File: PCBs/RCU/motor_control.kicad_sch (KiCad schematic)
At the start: 36 parts, among them U300 OPA365xxD, U301 DRV8876, U302 OPA365xxD, U303 DRV8876

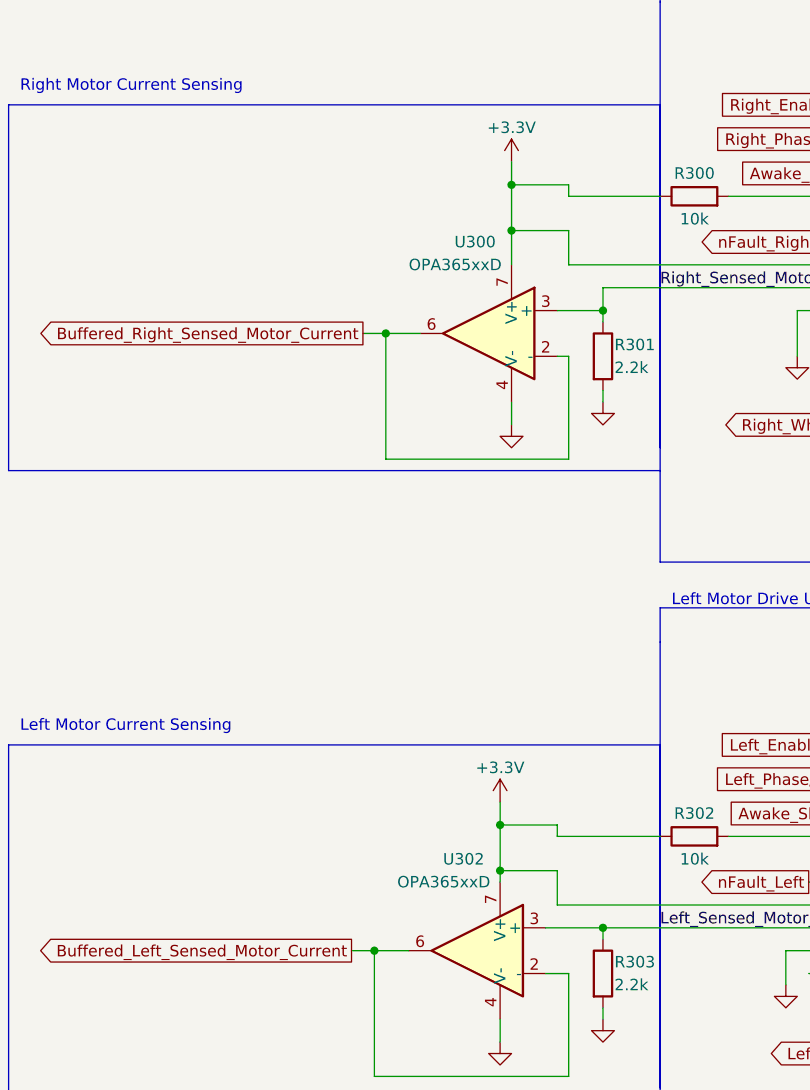
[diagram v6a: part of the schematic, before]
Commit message: Add 0.1uF bypass caps to Buffer in motor_control schematic
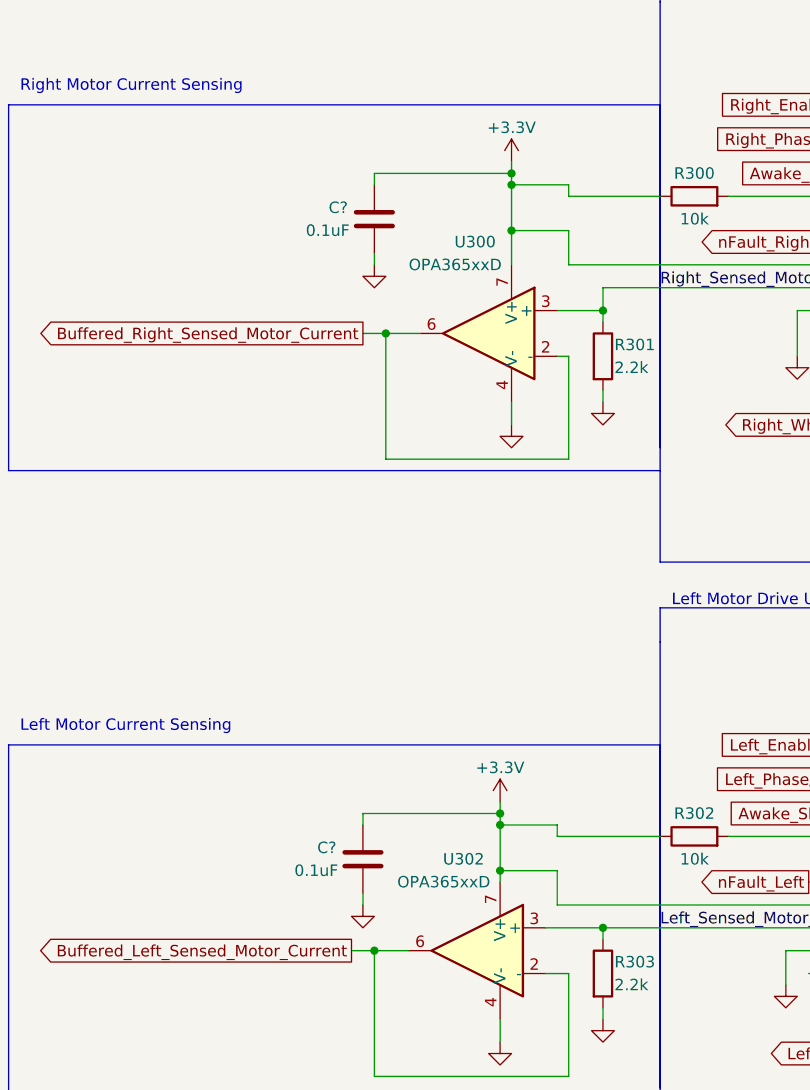
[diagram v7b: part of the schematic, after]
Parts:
- added C? (x2): 0.1uF, symbol Device:C
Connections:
- net +3V3: now also C?.1, C?.1
- net GND: now also C?.2, C?.2
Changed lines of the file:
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@@
   (junction (at 241.3 76.2) (diameter 0) (color 0 0 0 0)
   )
+  (junction (at 85.09 119.38) (diameter 0) (color 0 0 0 0)
+  )
   (junction (at 189.23 76.2) (diameter 0) (color 0 0 0 0)
   )
@@
   (junction (at 184.15 49.53) (diameter 0) (color 0 0 0 0)
   )
+  (junction (at 86.36 48.26) (diameter 0) (color 0 0 0 0)
+  )
   (junction (at 219.71 33.02) (diameter 0) (color 0 0 0 0)
   )
@@
     (stroke (width 0) (type default) (color 0 0 0 0))
   )
+  (wire (pts (xy 85.09 119.38) (xy 85.09 120.65))
+    (stroke (width 0) (type default) (color 0 0 0 0))
+  )
   (wire (pts (xy 193.04 146.05) (xy 193.04 147.32))
     (stroke (width 0) (type default) (color 0 0 0 0))
@@
     (stroke (width 0) (type default) (color 0 0 0 0))
   )
+  (wire (pts (xy 69.85 129.54) (xy 69.85 128.27))
+    (stroke (width 0) (type default) (color 0 0 0 0))
+  )
   (polyline (pts (xy 102.87 162.56) (xy 255.27 162.56))
     (stroke (width 0) (type default) (color 0 0 0 0))
@@
     (stroke (width 0) (type default) (color 0 0 0 0))
   )
+  (wire (pts (xy 71.12 48.26) (xy 86.36 48.26))
+    (stroke (width 0) (type default) (color 0 0 0 0))
+  )
   (wire (pts (xy 110.49 50.8) (xy 123.19 50.8))
     (stroke (width 0) (type default) (color 0 0 0 0))
@@
     (stroke (width 0) (type default) (color 0 0 0 0))
   )
+  (wire (pts (xy 69.85 119.38) (xy 85.09 119.38))
+    (stroke (width 0) (type default) (color 0 0 0 0))
+  )
   (wire (pts (xy 123.19 50.8) (xy 123.19 55.88))
     (stroke (width 0) (type default) (color 0 0 0 0))
@@
     (stroke (width 0) (type default) (color 0 0 0 0))
   )
+  (wire (pts (xy 86.36 48.26) (xy 86.36 49.53))
+    (stroke (width 0) (type default) (color 0 0 0 0))
+  )
   (polyline (pts (xy 30.48 40.64) (xy 102.87 40.64))
     (stroke (width 0) (type default) (color 0 0 0 0))
@@
     (stroke (width 0) (type default) (color 0 0 0 0))
   )
+  (wire (pts (xy 71.12 49.53) (xy 71.12 48.26))
+    (stroke (width 0) (type default) (color 0 0 0 0))
+  )
   (wire (pts (xy 189.23 132.08) (xy 189.23 134.62))
     (stroke (width 0) (type default) (color 0 0 0 0))
@@
     (stroke (width 0) (type default) (color 0 0 0 0))
   )
+  (wire (pts (xy 69.85 120.65) (xy 69.85 119.38))
+    (stroke (width 0) (type default) (color 0 0 0 0))
+  )
   (wire (pts (xy 128.27 119.38) (xy 128.27 111.76))
     (stroke (width 0) (type default) (color 0 0 0 0))
@@
     (stroke (width 0) (type default) (color 0 0 0 0))
   )
-  (wire (pts (xy 86.36 46.99) (xy 86.36 49.53))
+  (wire (pts (xy 86.36 46.99) (xy 86.36 48.26))
     (stroke (width 0) (type default) (color 0 0 0 0))
   )
@@
     (stroke (width 0) (type default) (color 0 0 0 0))
   )
-  (wire (pts (xy 85.09 118.11) (xy 85.09 120.65))
+  (wire (pts (xy 85.09 118.11) (xy 85.09 119.38))
     (stroke (width 0) (type default) (color 0 0 0 0))
   )
@@
   )
   (wire (pts (xy 92.71 50.8) (xy 92.71 49.53))
+    (stroke (width 0) (type default) (color 0 0 0 0))
+  )
+  (wire (pts (xy 71.12 58.42) (xy 71.12 57.15))
     (stroke (width 0) (type default) (color 0 0 0 0))
   )
@@
     )
   )
+  (symbol (lib_id "power:GND") (at 71.12 58.42 0) (unit 1)
+    (in_bom yes) (on_board yes) (fields_autoplaced)
+    (property "Reference" "#PWR?" (id 0) (at 71.12 64.77 0)
+      (effects (font (size 1.27 1.27)) hide)
+    )
+    (property "Value" "GND" (id 1) (at 71.12 63.5 0)
+      (effects (font (size 1.27 1.27)) hide)
+    )
+    (property "Footprint" "" (id 2) (at 71.12 58.42 0)
+      (effects (font (size 1.27 1.27)) hide)
+    )
+    (property "Datasheet" "" (id 3) (at 71.12 58.42 0)
+      (effects (font (size 1.27 1.27)) hide)
+    )
+    (pin "1")
+  )
   (symbol (lib_id "Device:R") (at 96.52 137.16 0) (unit 1)
     (in_bom yes) (on_board yes)
@@
     )
     (pin "1")
+  )
+  (symbol (lib_id "Device:C") (at 71.12 53.34 0) (unit 1)
+    (in_bom yes) (on_board yes)
+    (property "Reference" "C?" (id 0) (at 66.04 52.07 0)
+      (effects (font (size 1.27 1.27)) (justify left))
+    )
+    (property "Value" "0.1uF" (id 1) (at 63.5 54.61 0)
+      (effects (font (size 1.27 1.27)) (justify left))
+    )
+    (property "Footprint" "" (id 2) (at 72.0852 57.15 0)
+      (effects (font (size 1.27 1.27)) hide)
+    )
+    (property "Datasheet" "~" (id 3) (at 71.12 53.34 0)
+      (effects (font (size 1.27 1.27)) hide)
+    )
+    (pin "1")
+    (pin "2")
   )
   (symbol (lib_id "Ghanis_Symbols_KiCad6:DRV8876") (at 146.05 55.88 0) (unit 1)
@@
     (pin "1")
   )
+  (symbol (lib_id "power:GND") (at 69.85 129.54 0) (unit 1)
+    (in_bom yes) (on_board yes) (fields_autoplaced)
+    (property "Reference" "#PWR?" (id 0) (at 69.85 135.89 0)
+      (effects (font (size 1.27 1.27)) hide)
+    )
+    (property "Value" "GND" (id 1) (at 69.85 134.62 0)
+      (effects (font (size 1.27 1.27)) hide)
+    )
+    (property "Footprint" "" (id 2) (at 69.85 129.54 0)
+      (effects (font (size 1.27 1.27)) hide)
+    )
+    (property "Datasheet" "" (id 3) (at 69.85 129.54 0)
+      (effects (font (size 1.27 1.27)) hide)
+    )
+    (pin "1")
+  )
   (symbol (lib_id "power:GND") (at 191.77 48.26 0) (mirror y) (unit 1)
     (in_bom yes) (on_board yes) (fields_autoplaced)
@@
     (pin "1")
   )
+  (symbol (lib_id "Device:C") (at 69.85 124.46 0) (unit 1)
+    (in_bom yes) (on_board yes)
+    (property "Reference" "C?" (id 0) (at 64.77 123.19 0)
+      (effects (font (size 1.27 1.27)) (justify left))
+    )
+    (property "Value" "0.1uF" (id 1) (at 62.23 125.73 0)
+      (effects (font (size 1.27 1.27)) (justify left))
+    )
+    (property "Footprint" "" (id 2) (at 70.8152 128.27 0)
+      (effects (font (size 1.27 1.27)) hide)
+    )
+    (property "Datasheet" "~" (id 3) (at 69.85 124.46 0)
+      (effects (font (size 1.27 1.27)) hide)
+    )
+    (pin "1")
+    (pin "2")
+  )
   (symbol (lib_id "Ghanis_Symbols_KiCad6:DRV8876") (at 144.78 127 0) (unit 1)

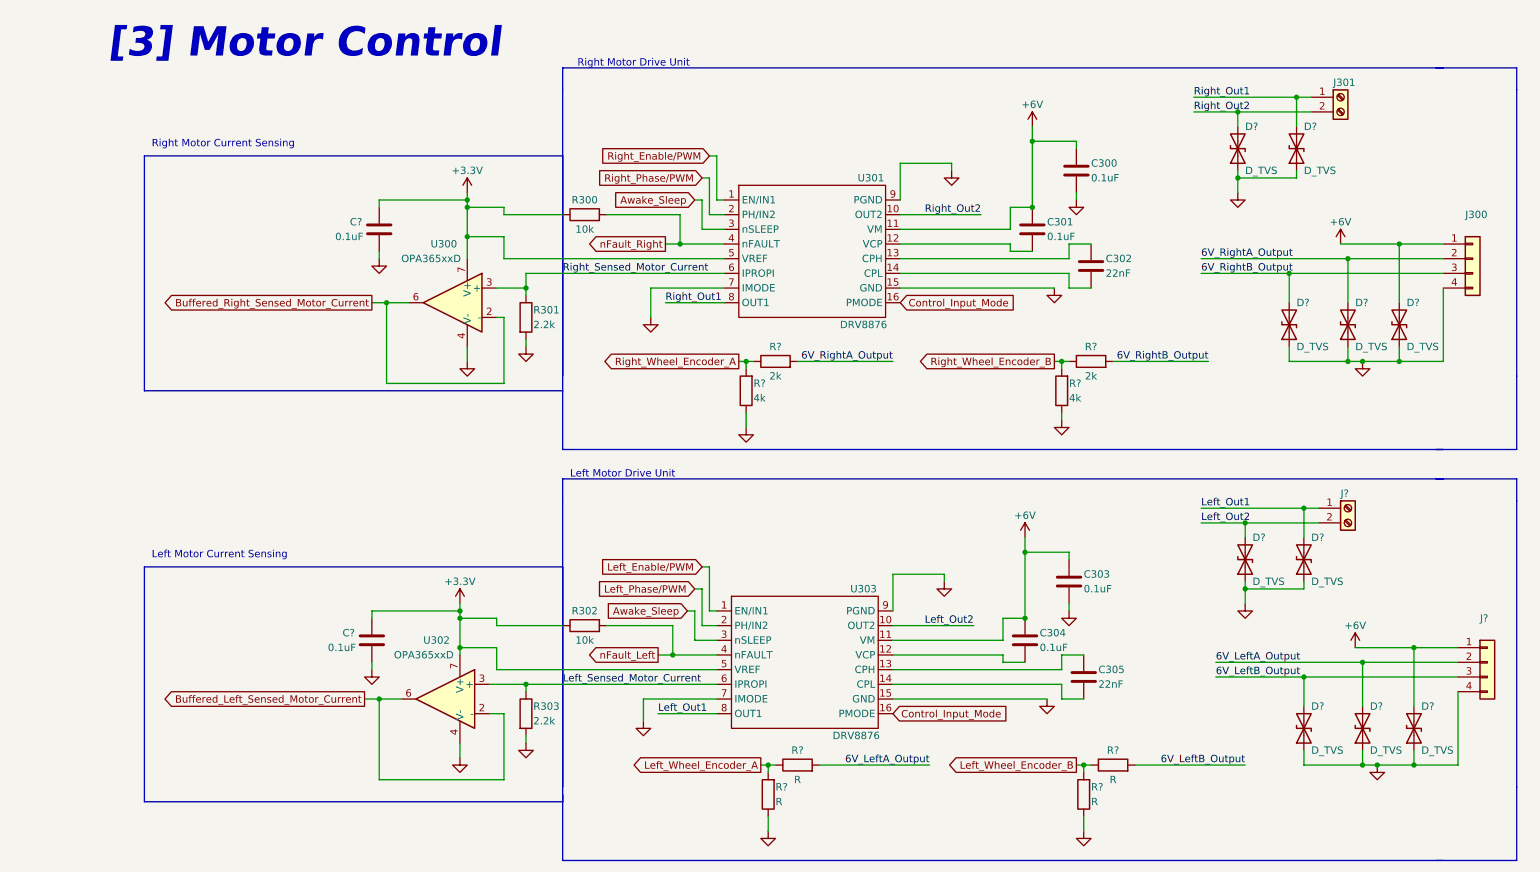
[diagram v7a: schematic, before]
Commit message: Corrected resistor values for stepping down encoder output voltage
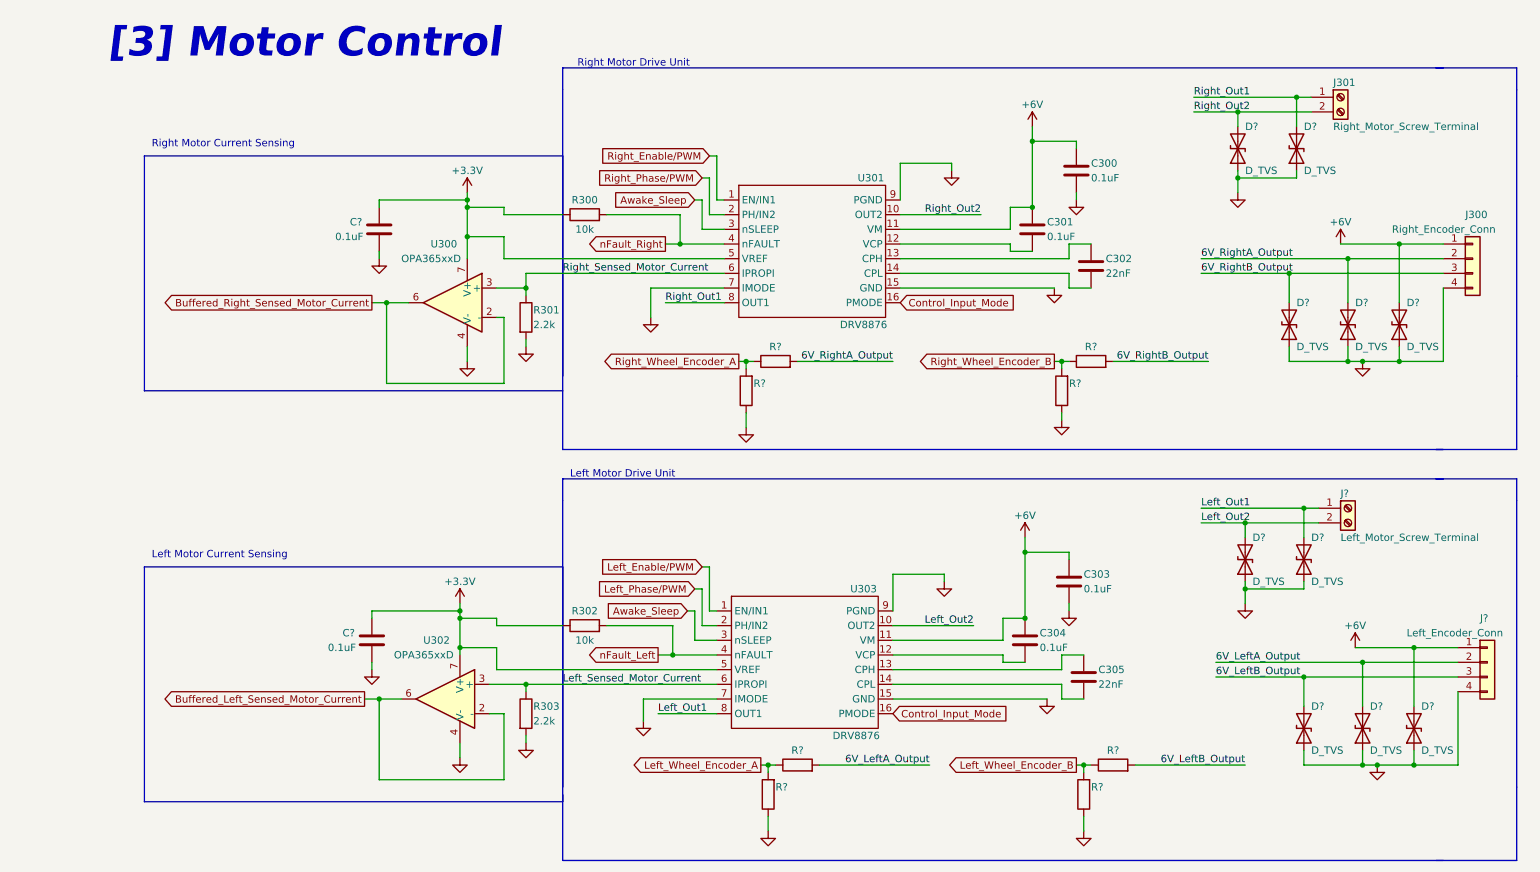
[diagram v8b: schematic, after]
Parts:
- J300: value (none) -> Right_Encoder_Conn
- J301: value (none) -> Right_Motor_Screw_Terminal
- J?: value (none) -> Left_Motor_Screw_Terminal
- J?: value (none) -> Left_Encoder_Conn
- R? (x2): value 4k -> (none)
- R? (x4): value R -> (none)
- R? (x2): value 2k -> (none)
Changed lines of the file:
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@@
       (effects (font (size 1.27 1.27)) (justify right))
     )
-    (property "Value" "4k" (id 1) (at 190.5 82.55 0)
+    (property "Value" "" (id 1) (at 190.5 82.55 0)
       (effects (font (size 1.27 1.27)) (justify right))
     )
@@
       (effects (font (size 1.27 1.27)) (justify right))
     )
-    (property "Value" "4k" (id 1) (at 135.89 82.55 0)
+    (property "Value" "" (id 1) (at 135.89 82.55 0)
       (effects (font (size 1.27 1.27)) (justify right))
     )
@@
       (effects (font (size 1.27 1.27)) (justify left))
     )
-    (property "Value" "" (id 1) (at 237.49 106.68 0)
+    (property "Value" "Left_Motor_Screw_Terminal" (id 1) (at 237.49 106.68 0)
       (effects (font (size 1.27 1.27)) (justify left))
     )
@@
     (in_bom yes) (on_board yes)
     (property "Reference" "R?" (id 0) (at 198.12 143.51 90))
-    (property "Value" "R" (id 1) (at 198.12 148.59 90))
+    (property "Value" "" (id 1) (at 198.12 148.59 90))
     (property "Footprint" "" (id 2) (at 198.12 147.828 90)
       (effects (font (size 1.27 1.27)) hide)
@@
       (effects (font (size 1.27 1.27)) (justify right))
     )
-    (property "Value" "R" (id 1) (at 194.31 152.4 0)
+    (property "Value" "" (id 1) (at 194.31 152.4 0)
       (effects (font (size 1.27 1.27)) (justify right))
     )
@@
     (in_bom yes) (on_board yes)
     (property "Reference" "R?" (id 0) (at 194.31 73.66 90))
-    (property "Value" "2k" (id 1) (at 194.31 78.74 90))
+    (property "Value" "" (id 1) (at 194.31 78.74 90))
     (property "Footprint" "" (id 2) (at 194.31 77.978 90)
       (effects (font (size 1.27 1.27)) hide)
@@
       (effects (font (size 1.27 1.27)) (justify right))
     )
-    (property "Value" "R" (id 1) (at 139.7 152.4 0)
+    (property "Value" "" (id 1) (at 139.7 152.4 0)
       (effects (font (size 1.27 1.27)) (justify right))
     )
@@
       (effects (font (size 1.27 1.27)) (justify left))
     )
-    (property "Value" "" (id 1) (at 236.22 35.56 0)
+    (property "Value" "Right_Motor_Screw_Terminal" (id 1) (at 236.22 35.56 0)
       (effects (font (size 1.27 1.27)) (justify left))
     )
@@
       (effects (font (size 1.27 1.27)) (justify left))
     )
-    (property "Value" "" (id 1) (at 248.92 123.19 0)
+    (property "Value" "Left_Encoder_Conn" (id 1) (at 248.92 123.19 0)
       (effects (font (size 1.27 1.27)) (justify left))
     )
@@
       (effects (font (size 1.27 1.27)) (justify left))
     )
-    (property "Value" "" (id 1) (at 246.38 53.34 0)
+    (property "Value" "Right_Encoder_Conn" (id 1) (at 246.38 53.34 0)
       (effects (font (size 1.27 1.27)) (justify left))
     )
@@
     (in_bom yes) (on_board yes)
     (property "Reference" "R?" (id 0) (at 139.7 73.66 90))
-    (property "Value" "2k" (id 1) (at 139.7 78.74 90))
+    (property "Value" "" (id 1) (at 139.7 78.74 90))
     (property "Footprint" "" (id 2) (at 139.7 77.978 90)
       (effects (font (size 1.27 1.27)) hide)
@@
     (in_bom yes) (on_board yes)
     (property "Reference" "R?" (id 0) (at 143.51 143.51 90))
-    (property "Value" "R" (id 1) (at 143.51 148.59 90))
+    (property "Value" "" (id 1) (at 143.51 148.59 90))
     (property "Footprint" "" (id 2) (at 143.51 147.828 90)
       (effects (font (size 1.27 1.27)) hide)
